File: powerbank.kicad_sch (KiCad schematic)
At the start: 24 parts

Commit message: da
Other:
- company: (none) -> TampanTech
- title: (none) -> PowerBank
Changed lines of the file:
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@@
 	(generator_version "8.0")
 	(paper "A4")
+	(title_block
+		(title "PowerBank")
+		(date "2024-09-08")
+		(rev "1")
+		(company "TampanTech")
+		(comment 1 "Drone Flight Management Unit")
+	)
 	(junction
 		(at 21.59 73.66)

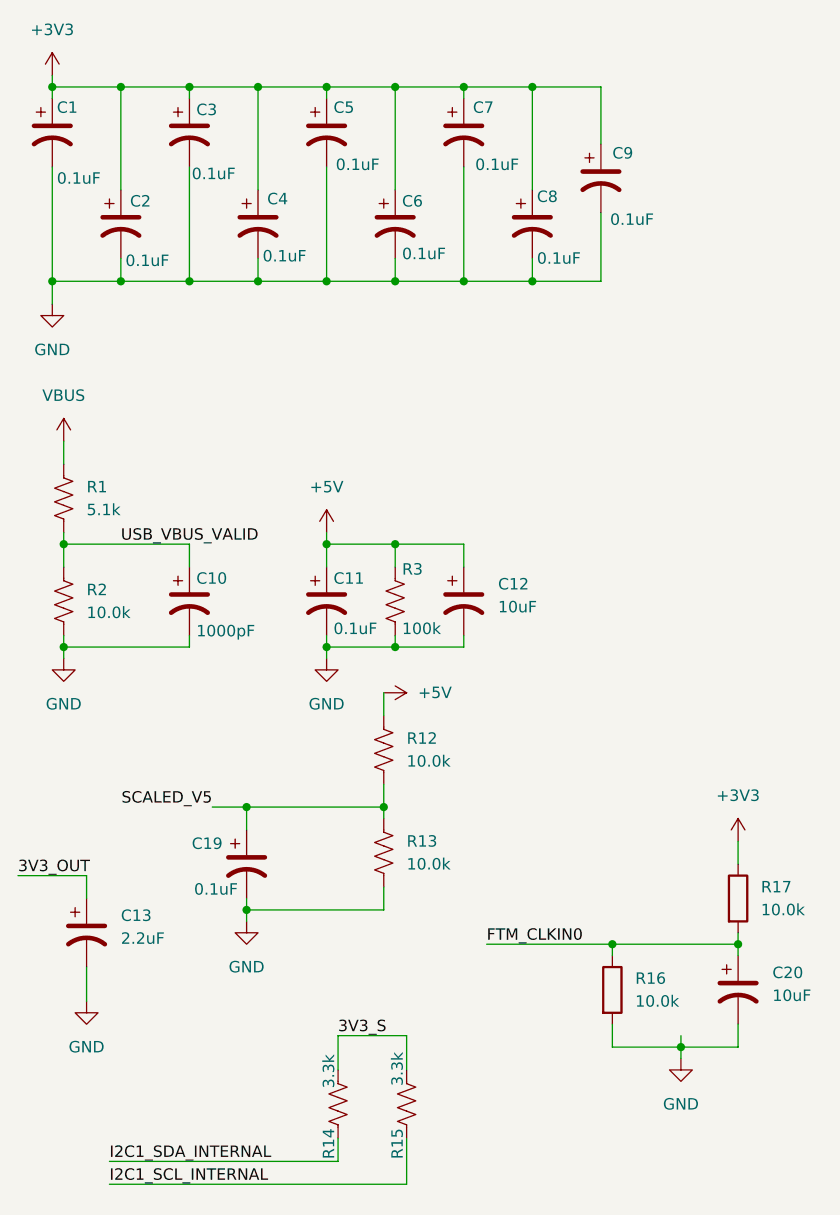
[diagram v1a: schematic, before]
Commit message: change label to global
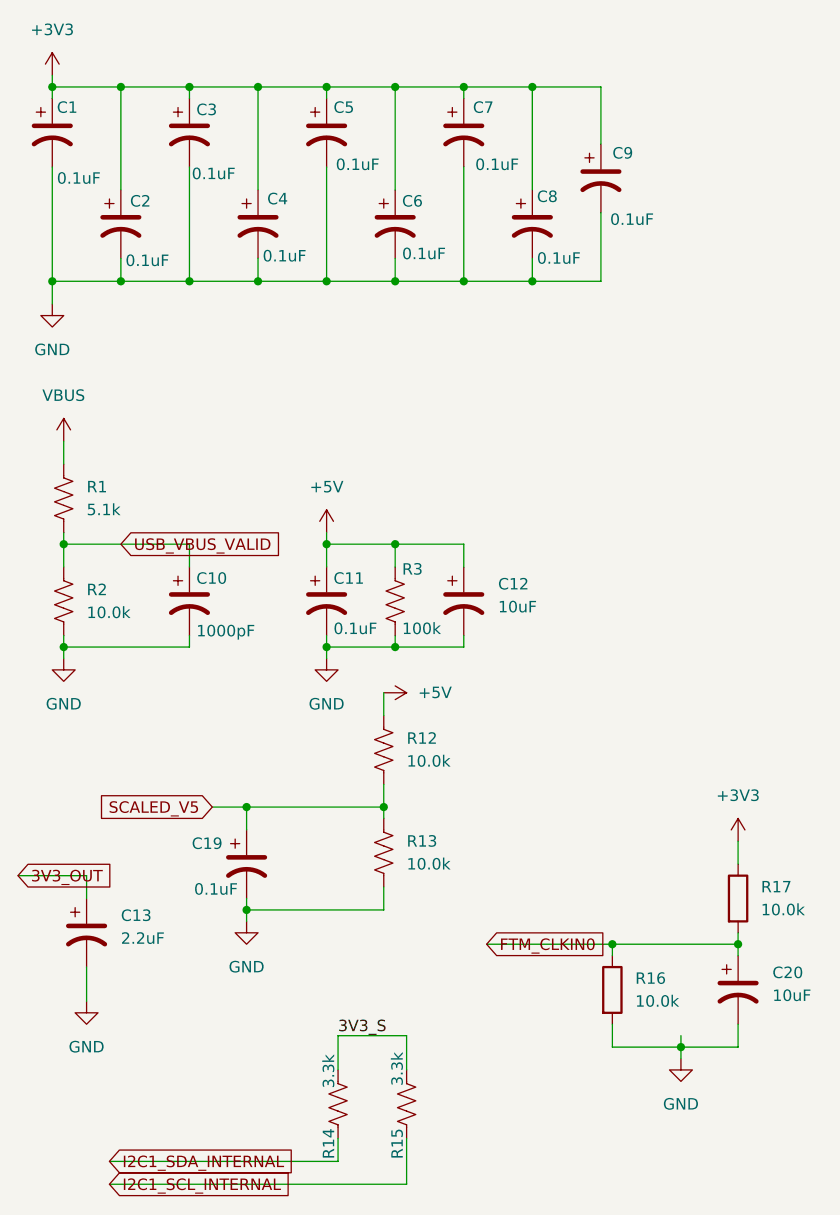
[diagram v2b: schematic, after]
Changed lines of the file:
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@@
-		)
-	)
-	(label "I2C1_SDA_INTERNAL"
-		(at 26.67 142.24 0)
-		(fields_autoplaced yes)
-		(effects
-			(font
-				(size 1.27 1.27)
-			)
-			(justify left bottom)
 		)
 	)
@@
 		)
 	)
-	(label "FTM_CLKIN0"
+	(global_label "FTM_CLKIN0"
+		(shape input)
 		(at 68.58 118.11 0)
 		(fields_autoplaced yes)
@@
 				(size 1.27 1.27)
 			)
-			(justify left bottom)
+			(justify left)
+		)
+		(property "Intersheetrefs" "${INTERSHEET_REFS}"
+			(at 82.7533 118.11 0)
+			(effects
+				(font
+					(size 1.27 1.27)
+				)
+				(justify left)
+				(hide yes)
+			)
 		)
 	)
-	(label "USB_VBUS_VALID"
+	(global_label "USB_VBUS_VALID"
+		(shape input)
 		(at 27.94 73.66 0)
 		(fields_autoplaced yes)
@@
 				(size 1.27 1.27)
 			)
-			(justify left bottom)
+			(justify left)
+		)
+		(property "Intersheetrefs" "${INTERSHEET_REFS}"
+			(at 46.6491 73.66 0)
+			(effects
+				(font
+					(size 1.27 1.27)
+				)
+				(justify left)
+				(hide yes)
+			)
 		)
 	)
-	(label "I2C1_SCL_INTERNAL"
+	(global_label "I2C1_SDA_INTERNAL"
+		(shape input)
+		(at 26.67 142.24 0)
+		(fields_autoplaced yes)
+		(effects
+			(font
+				(size 1.27 1.27)
+			)
+			(justify left)
+		)
+		(property "Intersheetrefs" "${INTERSHEET_REFS}"
+			(at 48.2214 142.24 0)
+			(effects
+				(font
+					(size 1.27 1.27)
+				)
+				(justify left)
+				(hide yes)
+			)
+		)
+	)
+	(global_label "I2C1_SCL_INTERNAL"
+		(shape input)
 		(at 26.67 144.78 0)
 		(fields_autoplaced yes)
@@
 				(size 1.27 1.27)
 			)
-			(justify left bottom)
+			(justify left)
+		)
+		(property "Intersheetrefs" "${INTERSHEET_REFS}"
+			(at 48.1609 144.78 0)
+			(effects
+				(font
+					(size 1.27 1.27)
+				)
+				(justify left)
+				(hide yes)
+			)
 		)
 	)
-	(label "3V3_OUT"
+	(global_label "SCALED_V5"
+		(shape input)
+		(at 38.1 102.87 180)
+		(fields_autoplaced yes)
+		(effects
+			(font
+				(size 1.27 1.27)
+			)
+			(justify right)
+		)
+		(property "Intersheetrefs" "${INTERSHEET_REFS}"
+			(at 24.8339 102.87 0)
+			(effects
+				(font
+					(size 1.27 1.27)
+				)
+				(justify right)
+				(hide yes)
+			)
+		)
+	)
+	(global_label "3V3_OUT"
+		(shape input)
 		(at 16.51 110.49 0)
 		(fields_autoplaced yes)
@@
 				(size 1.27 1.27)
 			)
-			(justify left bottom)
+			(justify left)
+		)
+		(property "Intersheetrefs" "${INTERSHEET_REFS}"
+			(at 27.599 110.49 0)
+			(effects
+				(font
+					(size 1.27 1.27)
+				)
+				(justify left)
+				(hide yes)
+			)
 		)
 	)
-	(label "SCALED_V5"
-		(at 38.1 102.87 180)
-		(fields_autoplaced yes)
-		(effects
-			(font
-				(size 1.27 1.27)
-			)
-			(justify right bottom)
-		)
-	)
